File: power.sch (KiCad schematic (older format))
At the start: 63 parts, among them J1 Conn_01x02_Male, J2 Conn_01x02_Male, U1 TLV76750, U2 AP63203WU, U3 MCP73123-22S, U4 LM73100, U5 LM73100

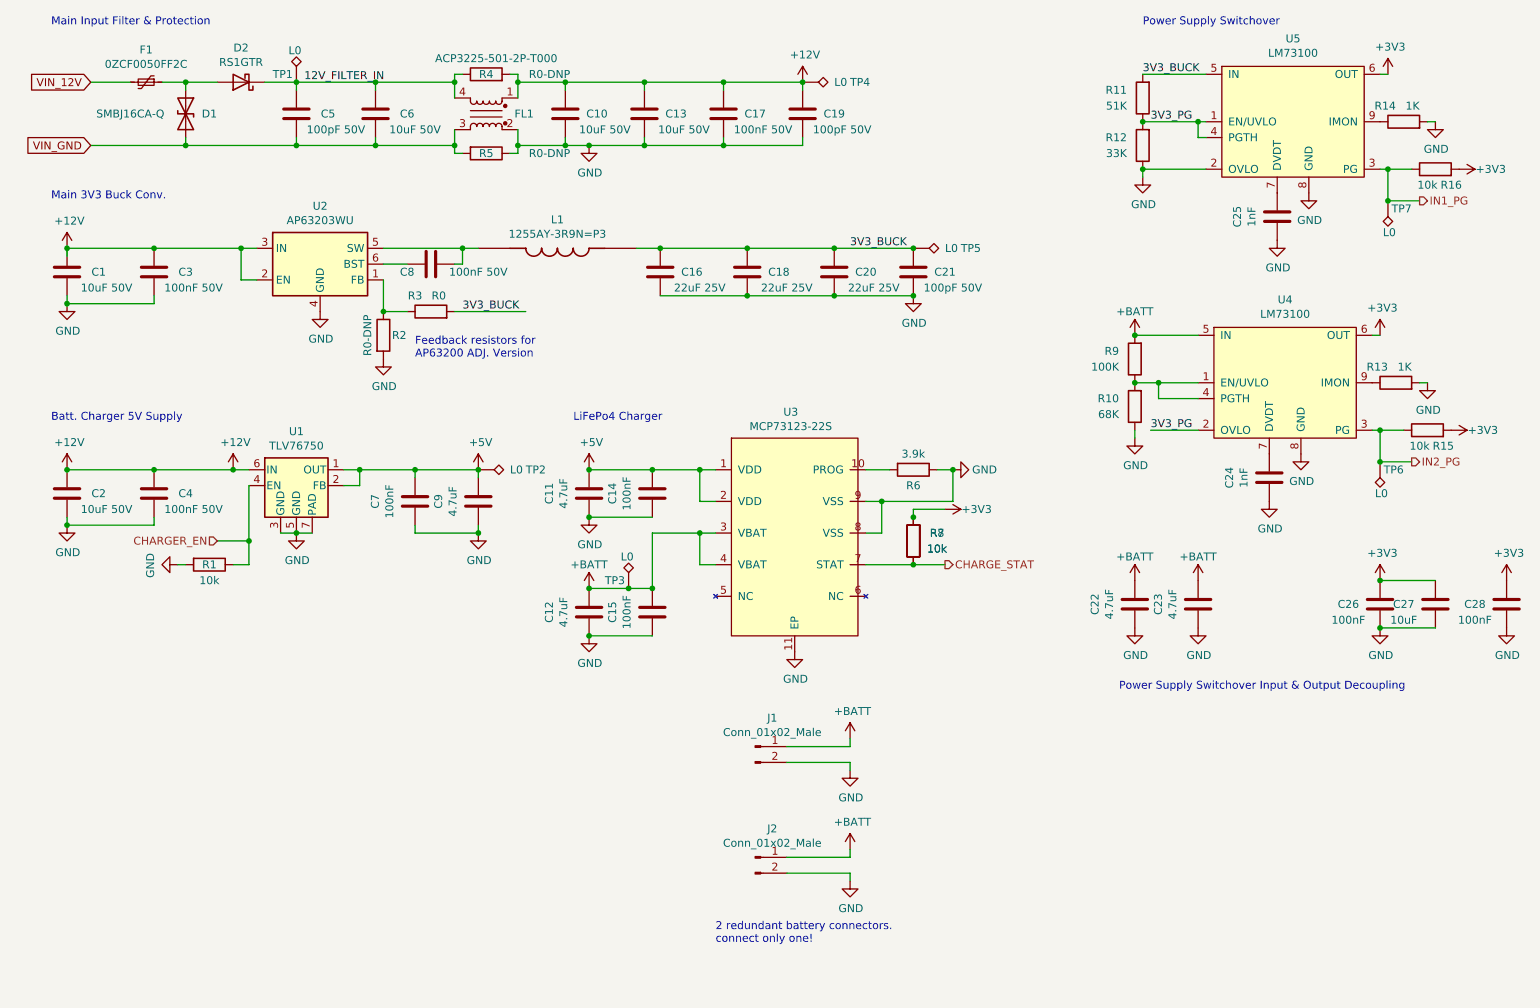
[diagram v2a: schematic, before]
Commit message: Power section placement completed.
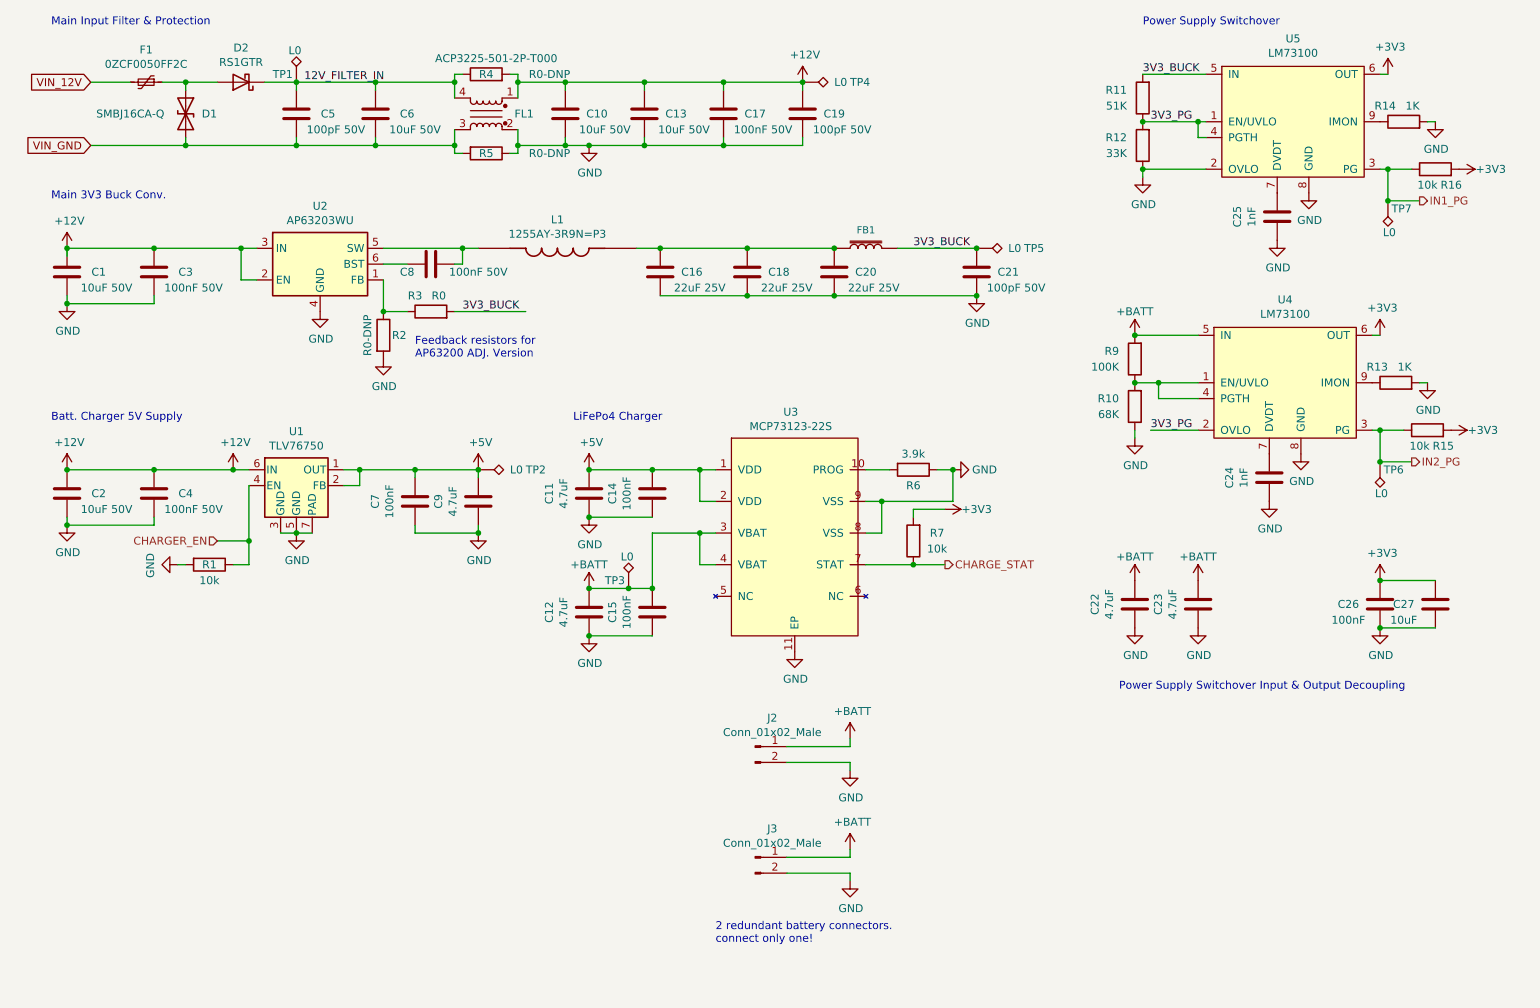
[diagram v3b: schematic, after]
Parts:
- removed C28: 100nF, Capacitor_SMD:C_0603_1608Metric, symbol Device:C
- removed R8: 10k, Resistors:0603, symbol Device:R
- added FB1: BLM18PG181SN1D, 0603, symbol SparkFun-Coils:FERRITE_BEAD-0603
- R1, R15, R16, R2, R3, R4, R5, R6, R7: footprint Resistors:0603 -> Resistor_SMD:R_0603_1608Metric
- TP1, TP2, TP3, TP4, TP5, TP6, TP7: footprint OLIMEX_TestPoints-FP:TP_SMD -> TestPoint:TestPoint_Pad_D1.0mm
- renumbered J1 to J2, J2 to J3
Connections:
- net 3V3_BUCK: now also FB1.2; no longer C16.2, C18.2, C20.2, L1.2
- new net: C16.2, C18.2, C20.2, FB1.1, L1.2
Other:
- moved on the sheet: C21, TP5
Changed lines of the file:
@@
 F 0 "R4" V 4000 1500 50  0000 C CNN
 F 1 "R0-DNP" V 4000 1100 50  0000 C CNN
-F 2 "Resistors:0603" V 3930 1500 50  0001 C CNN
+F 2 "Resistor_SMD:R_0603_1608Metric" V 3930 1500 50  0001 C CNN
 F 3 "~" H 4000 1500 50  0001 C CNN
 	1    4000 1500
@@
 F 0 "R5" V 4000 2000 50  0000 C CNN
 F 1 "R0-DNP" V 4000 2400 50  0000 C CNN
-F 2 "Resistors:0603" V 3930 2000 50  0001 C CNN
+F 2 "Resistor_SMD:R_0603_1608Metric" V 3930 2000 50  0001 C CNN
 F 3 "~" H 4000 2000 50  0001 C CNN
 	1    4000 2000
@@
 F 0 "R3" V 3750 3100 50  0000 C CNN
 F 1 "R0" V 3750 2950 50  0000 C CNN
-F 2 "Resistors:0603" V 3580 3000 50  0001 C CNN
+F 2 "Resistor_SMD:R_0603_1608Metric" V 3580 3000 50  0001 C CNN
 F 3 "~" H 3650 3000 50  0001 C CNN
 	1    3650 3000
@@
 F 0 "R2" H 3450 3150 50  0000 C CNN
 F 1 "R0-DNP" V 3250 3150 50  0000 C CNN
-F 2 "Resistors:0603" V 3280 3150 50  0001 C CNN
+F 2 "Resistor_SMD:R_0603_1608Metric" V 3280 3150 50  0001 C CNN
 F 3 "~" H 3350 3150 50  0001 C CNN
 	1    3350 3150
@@
 L Device:C C?
 U 1 1 60522F73
-P 6700 2750
+P 7100 2750
 AR Path="/60522F73" Ref="C?"  Part="1"
 AR Path="/60856F71/60522F73" Ref="C21"  Part="1"
-F 0 "C21" H 6500 2750 50  0000 C CNN
-F 1 "100pF 50V" H 6450 2850 50  0000 C CNN
-F 2 "Capacitor_SMD:C_0603_1608Metric" H 6738 2600 50  0001 C CNN
-F 3 "~" H 6700 2750 50  0001 C CNN
-	1    6700 2750
+F 0 "C21" H 6900 2750 50  0000 C CNN
+F 1 "100pF 50V" H 6850 2850 50  0000 C CNN
+F 2 "Capacitor_SMD:C_0603_1608Metric" H 7138 2600 50  0001 C CNN
+F 3 "~" H 7100 2750 50  0001 C CNN
+	1    7100 2750
 	-1   0    0    1
 $EndComp
@@
 Wire Wire Line
 	5650 2600 6200 2600
-Connection ~ 6200 2600
-Wire Wire Line
-	6200 2600 6700 2600
-Wire Wire Line
-	6700 2900 6200 2900
+Wire Wire Line
+	6600 2600 7100 2600
 Connection ~ 5650 2900
 Wire Wire Line
 	5650 2900 5100 2900
-Connection ~ 6200 2900
 Wire Wire Line
 	6200 2900 5650 2900
@@
 L power:GND #PWR?
 U 1 1 6052D387
-P 6700 2900
+P 7100 2900
 AR Path="/6052D387" Ref="#PWR?"  Part="1"
 AR Path="/60856F71/6052D387" Ref="#PWR023"  Part="1"
-F 0 "#PWR023" H 6700 2650 50  0001 C CNN
-F 1 "GND" H 6705 2727 50  0000 C CNN
-F 2 "" H 6700 2900 50  0001 C CNN
-F 3 "" H 6700 2900 50  0001 C CNN
-	1    6700 2900
-	1    0    0    -1
-$EndComp
-Connection ~ 6700 2900
+F 0 "#PWR023" H 7100 2650 50  0001 C CNN
+F 1 "GND" H 7105 2727 50  0000 C CNN
+F 2 "" H 7100 2900 50  0001 C CNN
+F 3 "" H 7100 2900 50  0001 C CNN
+	1    7100 2900
+	1    0    0    -1
+$EndComp
+Connection ~ 7100 2900
 Wire Wire Line
 	3350 2800 3350 3000
@@
 F 0 "R6" V 6800 4000 50  0000 C CNN
 F 1 "3.9k" V 6600 4000 50  0000 C CNN
-F 2 "Resistors:0603" V 6630 4000 50  0001 C CNN
+F 2 "Resistor_SMD:R_0603_1608Metric" V 6630 4000 50  0001 C CNN
 F 3 "~" H 6700 4000 50  0001 C CNN
 	1    6700 4000
@@
 F 0 "R7" H 6550 4400 50  0000 C CNN
 F 1 "10k" H 6550 4500 50  0000 C CNN
-F 2 "Resistors:0603" V 6630 4450 50  0001 C CNN
+F 2 "Resistor_SMD:R_0603_1608Metric" V 6630 4450 50  0001 C CNN
 F 3 "~" H 6700 4450 50  0001 C CNN
 	1    6700 4450
@@
 $Comp
 L Device:R R?
-U 1 1 60663BA3
-P 6700 4450
-AR Path="/60663BA3" Ref="R?"  Part="1"
-AR Path="/606146CD/60663BA3" Ref="R?"  Part="1"
-AR Path="/60856F71/60663BA3" Ref="R8"  Part="1"
-F 0 "R8" H 6550 4400 50  0000 C CNN
-F 1 "10k" H 6550 4500 50  0000 C CNN
-F 2 "Resistors:0603" V 6630 4450 50  0001 C CNN
-F 3 "~" H 6700 4450 50  0001 C CNN
-	1    6700 4450
-	-1   0    0    1
-$EndComp
-$Comp
-L Device:R R?
 U 1 1 60679B77
 P 2250 4600
@@
 F 0 "R1" V 2250 4600 50  0000 C CNN
 F 1 "10k" V 2350 4600 50  0000 C CNN
-F 2 "Resistors:0603" V 2180 4600 50  0001 C CNN
+F 2 "Resistor_SMD:R_0603_1608Metric" V 2180 4600 50  0001 C CNN
 F 3 "~" H 2250 4600 50  0001 C CNN
 	1    2250 4600
@@
 Connection ~ 5350 4000
 Connection ~ 5050 4000
-Text Label 6300 2600 0    50   ~ 0
+Text Label 6700 2600 0    50   ~ 0
 3V3_BUCK
 Wire Wire Line
 	6700 4300 6700 4250
-Connection ~ 6700 4300
 $Comp
 L power:GND #PWR?
@@
 $EndComp
 $Comp
-L Connector:Conn_01x02_Male J1
+L Connector:Conn_01x02_Male J2
 U 1 1 60560CAA
 P 5700 5750
-F 0 "J1" H 5808 5931 50  0000 C CNN
+F 0 "J2" H 5808 5931 50  0000 C CNN
 F 1 "Conn_01x02_Male" H 5808 5840 50  0000 C CNN
 F 2 "Connector_JST:JST_SH_BM02B-SRSS-TB_1x02-1MP_P1.00mm_Vertical" H 5700 5750 50  0001 C CNN
@@
 $EndComp
 $Comp
-L Connector:Conn_01x02_Male J2
+L Connector:Conn_01x02_Male J3
 U 1 1 60561025
 P 5700 6450
-F 0 "J2" H 5808 6631 50  0000 C CNN
+F 0 "J3" H 5808 6631 50  0000 C CNN
 F 1 "Conn_01x02_Male" H 5808 6540 50  0000 C CNN
 F 2 "Connector_JST:JST_SH_SM02B-SRSS-TB_1x02-1MP_P1.00mm_Horizontal" H 5700 6450 50  0001 C CNN
@@
 F 0 "TP2" V 3950 4300 50  0000 L CNN
 F 1 "L0" V 3950 4200 50  0000 L CNN
-F 2 "OLIMEX_TestPoints-FP:TP_SMD" H 4150 4000 50  0001 C CNN
+F 2 "TestPoint:TestPoint_Pad_D1.0mm" H 4150 4000 50  0001 C CNN
 F 3 "~" H 4150 4000 50  0001 C CNN
 	1    3950 4000
@@
 L Connector:TestPoint_Alt TP?
 U 1 1 60933923
-P 6700 2600
+P 7100 2600
 AR Path="/60933923" Ref="TP?"  Part="1"
 AR Path="/6055B0F2/60933923" Ref="TP?"  Part="1"
 AR Path="/60856F71/60933923" Ref="TP5"  Part="1"
-F 0 "TP5" V 6700 2900 50  0000 L CNN
-F 1 "L0" V 6700 2800 50  0000 L CNN
-F 2 "OLIMEX_TestPoints-FP:TP_SMD" H 6900 2600 50  0001 C CNN
-F 3 "~" H 6900 2600 50  0001 C CNN
-	1    6700 2600
+F 0 "TP5" V 7100 2900 50  0000 L CNN
+F 1 "L0" V 7100 2800 50  0000 L CNN
+F 2 "TestPoint:TestPoint_Pad_D1.0mm" H 7300 2600 50  0001 C CNN
+F 3 "~" H 7300 2600 50  0001 C CNN
+	1    7100 2600
 	0    1    1    0
 $EndComp
-Connection ~ 6700 2600
+Connection ~ 7100 2600
 $Comp
 L Connector:TestPoint_Alt TP?
@@
 F 0 "TP4" V 6000 1850 50  0000 L CNN
 F 1 "L0" V 6000 1750 50  0000 L CNN
-F 2 "OLIMEX_TestPoints-FP:TP_SMD" H 6200 1550 50  0001 C CNN
+F 2 "TestPoint:TestPoint_Pad_D1.0mm" H 6200 1550 50  0001 C CNN
 F 3 "~" H 6200 1550 50  0001 C CNN
 	1    6000 1550
@@
 F 0 "TP1" H 2650 1600 50  0000 L CNN
 F 1 "L0" H 2750 1750 50  0000 L CNN
-F 2 "OLIMEX_TestPoints-FP:TP_SMD" H 3000 1550 50  0001 C CNN
+F 2 "TestPoint:TestPoint_Pad_D1.0mm" H 3000 1550 50  0001 C CNN
 F 3 "~" H 3000 1550 50  0001 C CNN
 	1    2800 1550
@@
 F 0 "TP3" H 4750 4800 50  0000 L CNN
 F 1 "L0" H 4850 4950 50  0000 L CNN
-F 2 "OLIMEX_TestPoints-FP:TP_SMD" H 5100 4750 50  0001 C CNN
+F 2 "TestPoint:TestPoint_Pad_D1.0mm" H 5100 4750 50  0001 C CNN
 F 3 "~" H 5100 4750 50  0001 C CNN
 	1    4900 4750
@@
 Wire Wire Line
 	10000 5000 9650 5000
-$Comp
-L power:GND #PWR?
-U 1 1 605C2955
-P 10450 5000
-AR Path="/605C2955" Ref="#PWR?"  Part="1"
-AR Path="/60856F71/605C2955" Ref="#PWR046"  Part="1"
-F 0 "#PWR046" H 10450 4750 50  0001 C CNN
-F 1 "GND" H 10455 4827 50  0000 C CNN
-F 2 "" H 10450 5000 50  0001 C CNN
-F 3 "" H 10450 5000 50  0001 C CNN
-	1    10450 5000
-	1    0    0    -1
-$EndComp
-$Comp
-L Device:C C?
-U 1 1 605C295B
-P 10450 4850
-AR Path="/605C295B" Ref="C?"  Part="1"
-AR Path="/606146CD/605C295B" Ref="C?"  Part="1"
-AR Path="/603B75FA/605C295B" Ref="C?"  Part="1"
-AR Path="/60856F71/605C295B" Ref="C28"  Part="1"
-F 0 "C28" H 10250 4850 50  0000 C CNN
-F 1 "100nF" H 10250 4750 50  0000 C CNN
-F 2 "Capacitor_SMD:C_0603_1608Metric" H 10488 4700 50  0001 C CNN
-F 3 "~" H 10450 4850 50  0001 C CNN
-	1    10450 4850
-	1    0    0    -1
-$EndComp
-$Comp
-L power:+3V3 #PWR?
-U 1 1 605C2961
-P 10450 4700
-AR Path="/606146CD/605C2961" Ref="#PWR?"  Part="1"
-AR Path="/603B75FA/605C2961" Ref="#PWR?"  Part="1"
-AR Path="/603BB897/605C2961" Ref="#PWR?"  Part="1"
-AR Path="/6055B0F2/605C2961" Ref="#PWR?"  Part="1"
-AR Path="/60856F71/605C2961" Ref="#PWR045"  Part="1"
-F 0 "#PWR045" H 10450 4550 50  0001 C CNN
-F 1 "+3V3" H 10465 4873 50  0000 C CNN
-F 2 "" H 10450 4700 50  0001 C CNN
-F 3 "" H 10450 4700 50  0001 C CNN
-	1    10450 4700
-	1    0    0    -1
-$EndComp
 Connection ~ 9650 5000
 Wire Wire Line
@@
 F 0 "TP7" H 9550 2350 50  0000 L CNN
 F 1 "L0" H 9650 2500 50  0000 L CNN
-F 2 "OLIMEX_TestPoints-FP:TP_SMD" H 9900 2300 50  0001 C CNN
+F 2 "TestPoint:TestPoint_Pad_D1.0mm" H 9900 2300 50  0001 C CNN
 F 3 "~" H 9900 2300 50  0001 C CNN
 	1    9700 2300
@@
 F 0 "R15" V 9850 3650 50  0000 C CNN
 F 1 "10k" V 9850 3800 50  0000 C CNN
-F 2 "Resistors:0603" V 9880 3750 50  0001 C CNN
+F 2 "Resistor_SMD:R_0603_1608Metric" V 9880 3750 50  0001 C CNN
 F 3 "~" H 9950 3750 50  0001 C CNN
 	1    9950 3750
@@
 F 0 "R16" V 9900 2000 50  0000 C CNN
 F 1 "10k" V 9900 2150 50  0000 C CNN
-F 2 "Resistors:0603" V 9930 2100 50  0001 C CNN
+F 2 "Resistor_SMD:R_0603_1608Metric" V 9930 2100 50  0001 C CNN
 F 3 "~" H 10000 2100 50  0001 C CNN
 	1    10000 2100
@@
 F 0 "TP6" H 9500 4000 50  0000 L CNN
 F 1 "L0" H 9600 4150 50  0000 L CNN
-F 2 "OLIMEX_TestPoints-FP:TP_SMD" H 9850 3950 50  0001 C CNN
+F 2 "TestPoint:TestPoint_Pad_D1.0mm" H 9850 3950 50  0001 C CNN
 F 3 "~" H 9850 3950 50  0001 C CNN
 	1    9650 3950
@@
 Text Notes 8000 5400 0    50   ~ 0
 Power Supply Switchover Input & Output Decoupling
+$Comp
+L SparkFun-Coils:FERRITE_BEAD-0603 FB1
+U 1 1 6054698B
+P 6400 2600
+F 0 "FB1" V 6515 2600 45  0000 C CNN
+F 1 "BLM18PG181SN1D" V 6515 2600 45  0001 C CNN
+F 2 "0603" H 6400 2900 20  0001 C CNN
+F 3 "" H 6400 2600 50  0001 C CNN
+	1    6400 2600
+	0    -1   -1   0
+$EndComp
+Connection ~ 6200 2600
+Wire Wire Line
+	6200 2900 7100 2900
+Connection ~ 6200 2900
 $EndSCHEMATC

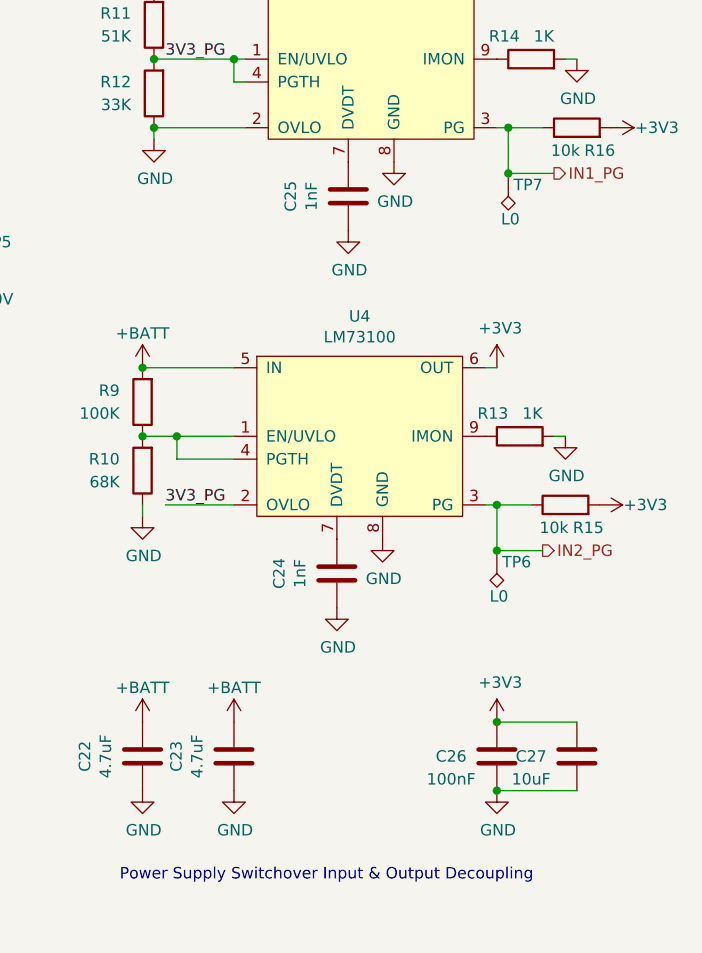
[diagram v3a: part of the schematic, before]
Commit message: Power section routing completed.
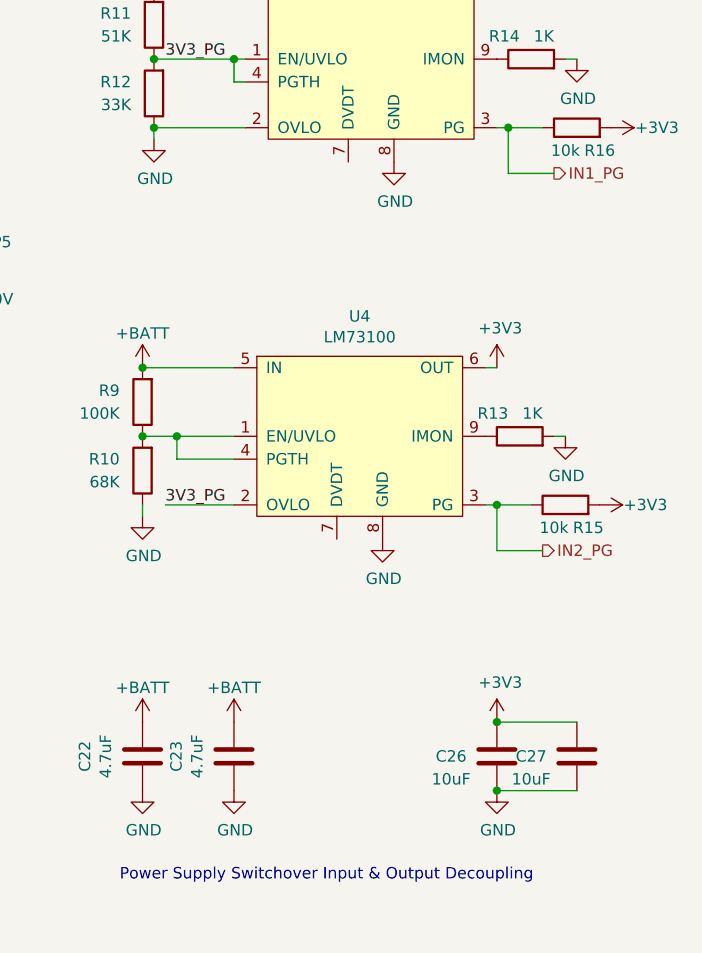
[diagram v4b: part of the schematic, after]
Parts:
- removed C24, C25: 1nF, Capacitor_SMD:C_0603_1608Metric, symbol Device:C
- removed TP6, TP7: L0, TestPoint:TestPoint_Pad_D1.0mm, symbol Connector:TestPoint_Alt
- C26: value 100nF -> 10uF
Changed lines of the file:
@@
-$EndComp
-$Comp
-L Device:C C?
-U 1 1 60415DFF
-P 9000 2400
-AR Path="/60415DFF" Ref="C?"  Part="1"
-AR Path="/603B75FA/60415DFF" Ref="C?"  Part="1"
-AR Path="/606146CD/60415DFF" Ref="C?"  Part="1"
-AR Path="/60856F71/60415DFF" Ref="C25"  Part="1"
-F 0 "C25" V 8748 2400 50  0000 C CNN
-F 1 "1nF" V 8839 2400 50  0000 C CNN
-F 2 "Capacitor_SMD:C_0603_1608Metric" H 9038 2250 50  0001 C CNN
-F 3 "~" H 9000 2400 50  0001 C CNN
-	1    9000 2400
-	1    0    0    -1
 $EndComp
 $Comp
@@
 $Comp
 L power:GND #PWR?
-U 1 1 6043BA6C
-P 9000 2550
-AR Path="/6043BA6C" Ref="#PWR?"  Part="1"
-AR Path="/60856F71/6043BA6C" Ref="#PWR034"  Part="1"
-F 0 "#PWR034" H 9000 2300 50  0001 C CNN
-F 1 "GND" H 9005 2377 50  0000 C CNN
-F 2 "" H 9000 2550 50  0001 C CNN
-F 3 "" H 9000 2550 50  0001 C CNN
-	1    9000 2550
-	1    0    0    -1
-$EndComp
-$Comp
-L Device:C C?
-U 1 1 6043C455
-P 8950 4050
-AR Path="/6043C455" Ref="C?"  Part="1"
-AR Path="/603B75FA/6043C455" Ref="C?"  Part="1"
-AR Path="/606146CD/6043C455" Ref="C?"  Part="1"
-AR Path="/60856F71/6043C455" Ref="C24"  Part="1"
-F 0 "C24" V 8698 4050 50  0000 C CNN
-F 1 "1nF" V 8789 4050 50  0000 C CNN
-F 2 "Capacitor_SMD:C_0603_1608Metric" H 8988 3900 50  0001 C CNN
-F 3 "~" H 8950 4050 50  0001 C CNN
-	1    8950 4050
-	1    0    0    -1
-$EndComp
-$Comp
-L power:GND #PWR?
 U 1 1 6043C45B
 P 9150 3900
@@
 F 3 "" H 9150 3900 50  0001 C CNN
 	1    9150 3900
-	1    0    0    -1
-$EndComp
-$Comp
-L power:GND #PWR?
-U 1 1 6043C461
-P 8950 4200
-AR Path="/6043C461" Ref="#PWR?"  Part="1"
-AR Path="/60856F71/6043C461" Ref="#PWR033"  Part="1"
-F 0 "#PWR033" H 8950 3950 50  0001 C CNN
-F 1 "GND" H 8955 4027 50  0000 C CNN
-F 2 "" H 8950 4200 50  0001 C CNN
-F 3 "" H 8950 4200 50  0001 C CNN
-	1    8950 4200
 	1    0    0    -1
 $EndComp
@@
 AR Path="/60856F71/605AB4FB" Ref="C26"  Part="1"
 F 0 "C26" H 9450 4850 50  0000 C CNN
-F 1 "100nF" H 9450 4750 50  0000 C CNN
+F 1 "10uF" H 9450 4750 50  0000 C CNN
 F 2 "Capacitor_SMD:C_0603_1608Metric" H 9688 4700 50  0001 C CNN
 F 3 "~" H 9650 4850 50  0001 C CNN
@@
 	8150 2100 8550 2100
 Connection ~ 8150 2100
-$Comp
-L Connector:TestPoint_Alt TP?
-U 1 1 605DAA2E
-P 9700 2300
-AR Path="/605DAA2E" Ref="TP?"  Part="1"
-AR Path="/6055B0F2/605DAA2E" Ref="TP?"  Part="1"
-AR Path="/60856F71/605DAA2E" Ref="TP7"  Part="1"
-F 0 "TP7" H 9550 2350 50  0000 L CNN
-F 1 "L0" H 9650 2500 50  0000 L CNN
-F 2 "TestPoint:TestPoint_Pad_D1.0mm" H 9900 2300 50  0001 C CNN
-F 3 "~" H 9900 2300 50  0001 C CNN
-	1    9700 2300
-	-1   0    0    1
-$EndComp
 $Comp
 L Device:R R?
@@
 Wire Wire Line
 	9700 2300 9900 2300
-Connection ~ 9700 2300
-$Comp
-L Connector:TestPoint_Alt TP?
-U 1 1 606698A5
-P 9650 3950
-AR Path="/606698A5" Ref="TP?"  Part="1"
-AR Path="/6055B0F2/606698A5" Ref="TP?"  Part="1"
-AR Path="/60856F71/606698A5" Ref="TP6"  Part="1"
-F 0 "TP6" H 9500 4000 50  0000 L CNN
-F 1 "L0" H 9600 4150 50  0000 L CNN
-F 2 "TestPoint:TestPoint_Pad_D1.0mm" H 9850 3950 50  0001 C CNN
-F 3 "~" H 9850 3950 50  0001 C CNN
-	1    9650 3950
-	-1   0    0    1
-$EndComp
 Text HLabel 9850 3950 2    50   Output ~ 0
 IN2_PG
@@
 Wire Wire Line
 	9650 3950 9850 3950
-Connection ~ 9650 3950
 $Comp
 L Device:C C?
